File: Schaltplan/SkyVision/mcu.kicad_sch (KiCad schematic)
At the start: 10 parts, among them U1 PIC16F690-ISO, X1 Crystal 20kHz

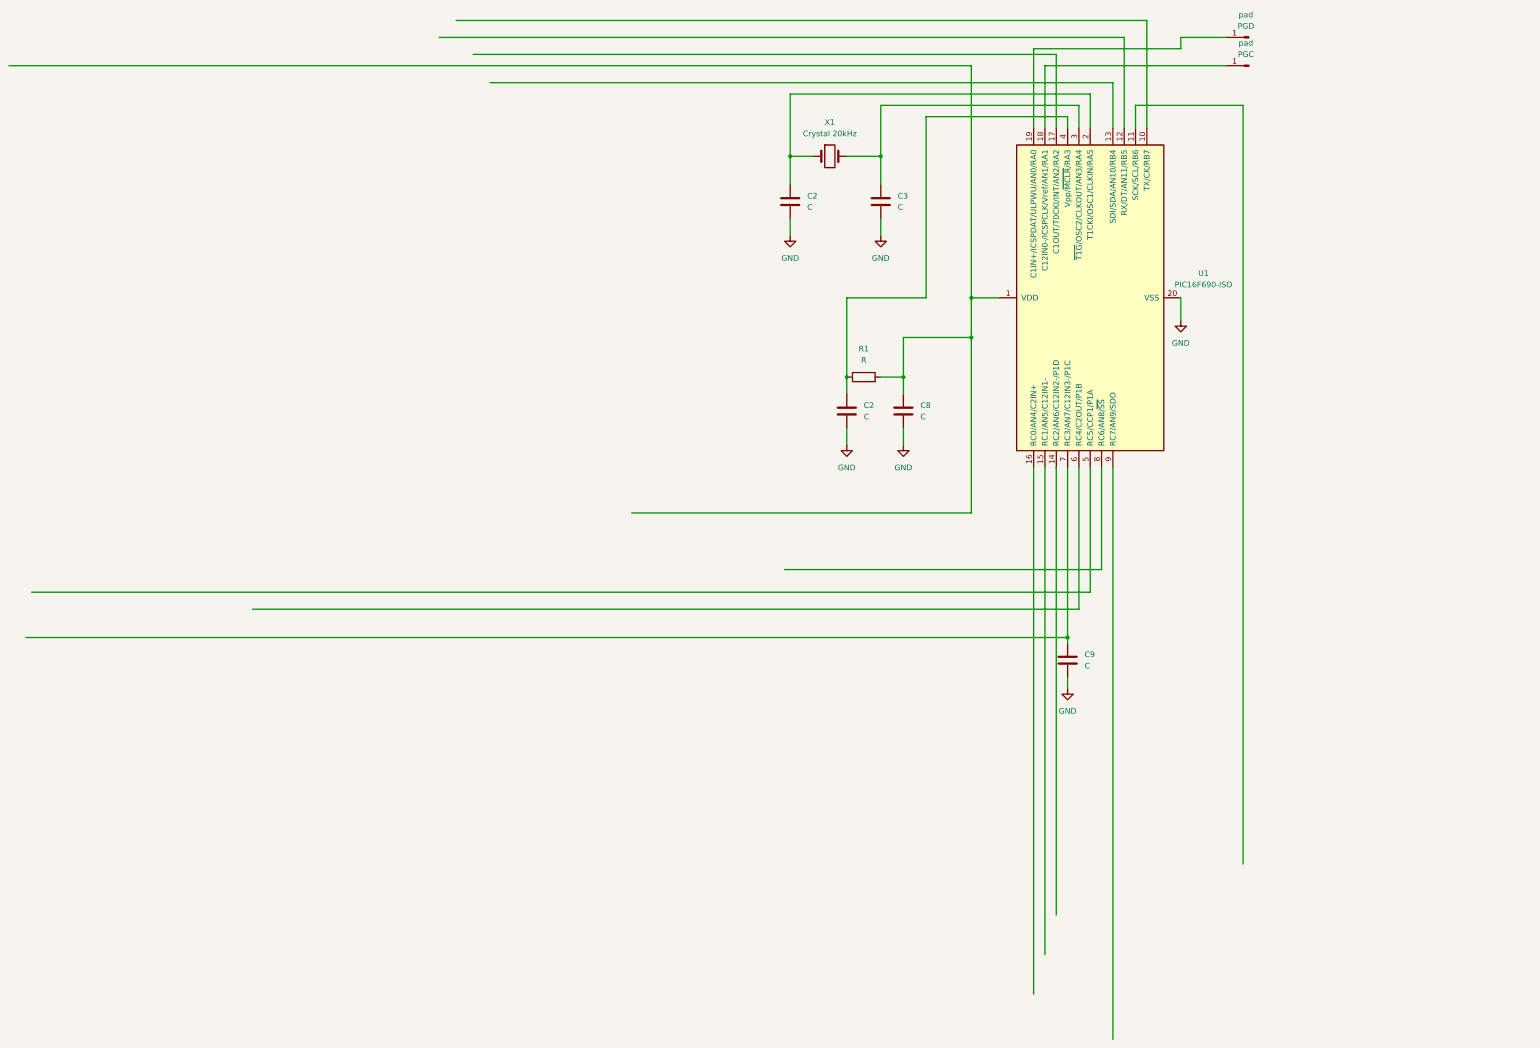
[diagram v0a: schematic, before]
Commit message: Schaltplan aufgeräumt
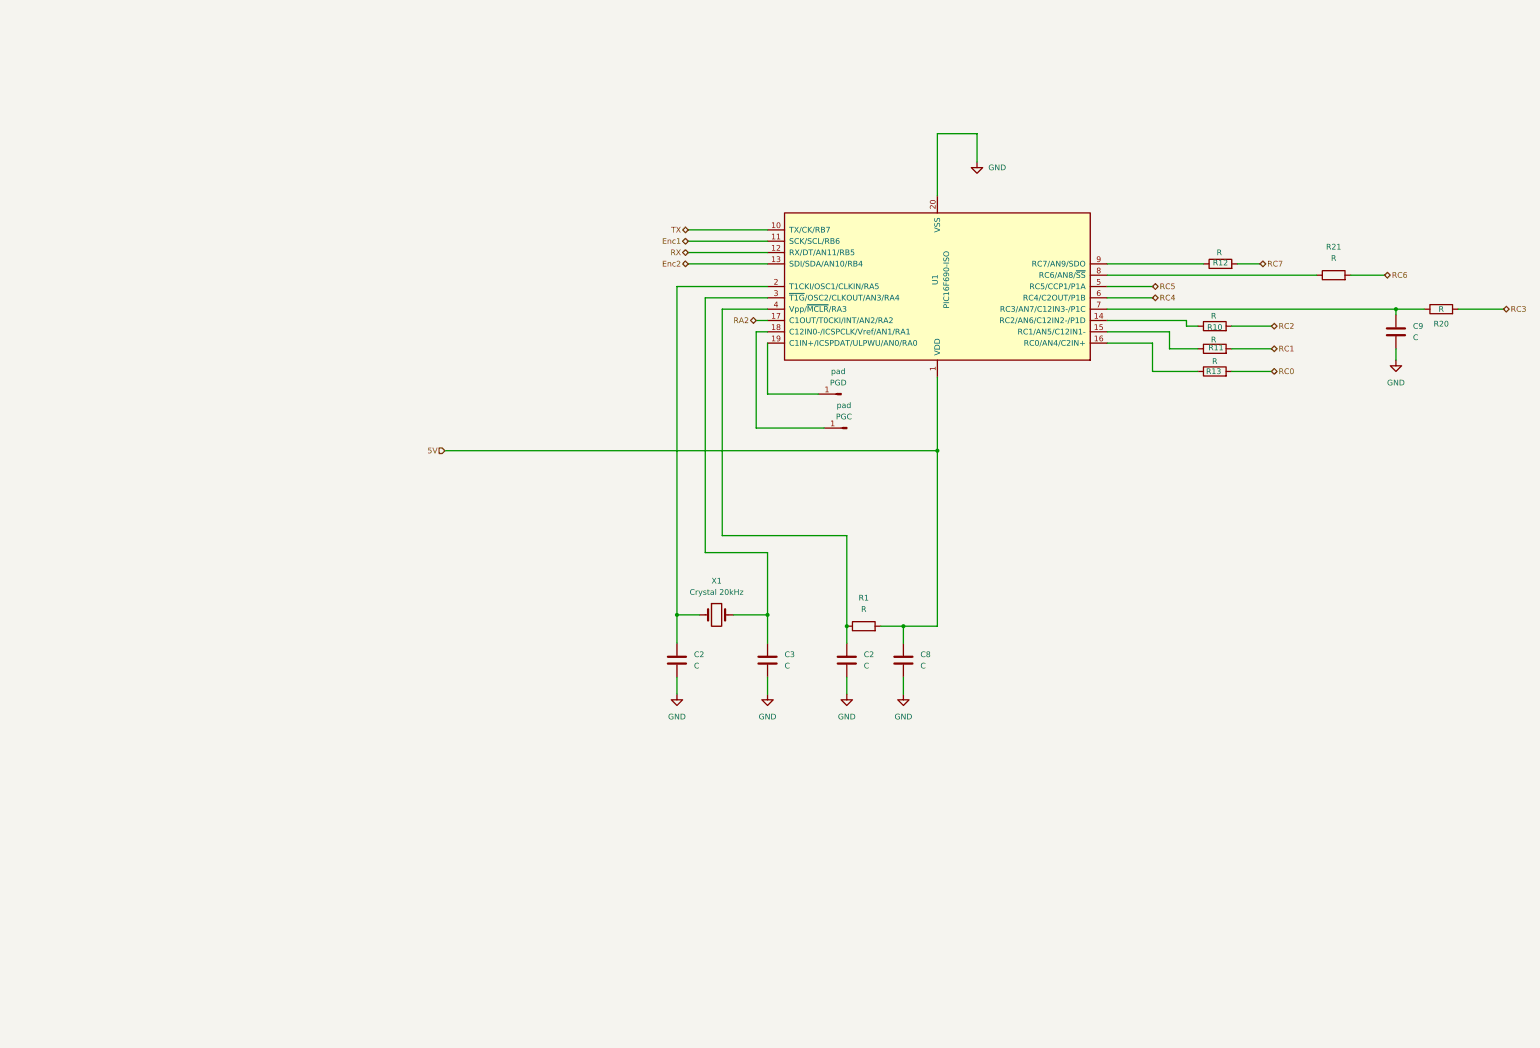
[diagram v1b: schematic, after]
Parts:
- added R10, R11, R12, R13, R20, R21: R, symbol Device:R
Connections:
- net 5V: now reaches C8.1, R1.2, U1.1 (VDD)
- net TX: now reaches U1.10 (TX/CK/RB7)
- net Enc1: now reaches U1.11 (SCK/SCL/RB6)
- net RX: now reaches U1.12 (RX/DT/AN11/RB5)
- net Enc2: now reaches U1.13 (SDI/SDA/AN10/RB4)
- net at U1.14 (RC2/AN6/C12IN2-/P1D): now also R10.1
- net at U1.15 (RC1/AN5/C12IN1-): now also R11.1
- net at U1.16 (RC0/AN4/C2IN+): now also R13.1
- net RA2: now reaches U1.17 (C1OUT/T0CKI/INT/AN2/RA2)
- net RC5: now reaches U1.5 (RC5/CCP1/P1A)
- net RC4: now reaches U1.6 (RC4/C2OUT/P1B)
- net at C9.1, U1.7 (RC3/AN7/C12IN3-/P1C): now also R20.1
- net at U1.8 (RC6/AN8/~{SS}): now also R21.1
- net at U1.9 (RC7/AN9/SDO): now also R12.1
- new net RC0: R13.2
- new net RC1: R11.2
- new net RC2: R10.2
- new net RC3: R20.2
- new net RC6: R21.2
- new net RC7: R12.2
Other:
- moved on the sheet: C2, C3, C8, C9, R1, U1, X1, pad
